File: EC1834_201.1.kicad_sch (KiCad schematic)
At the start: 91 parts, among them X6 RESET_BTN

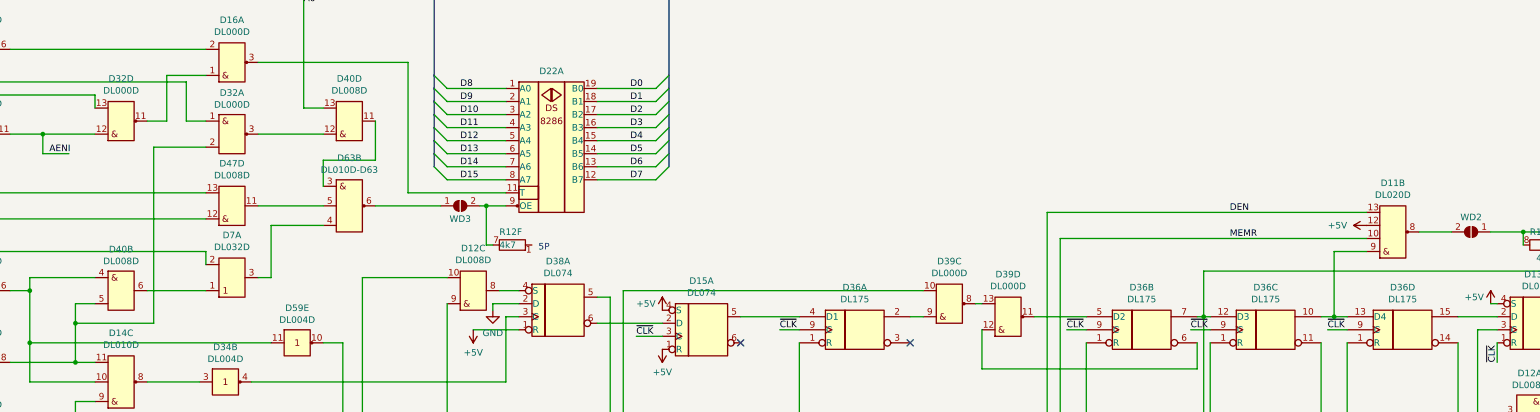
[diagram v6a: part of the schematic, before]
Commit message: Small optical changes
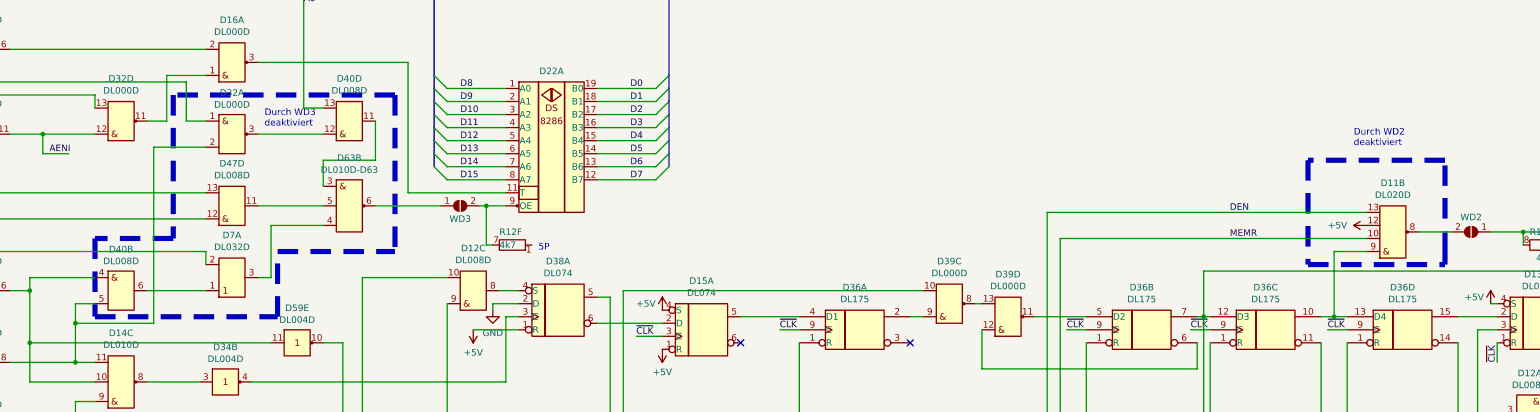
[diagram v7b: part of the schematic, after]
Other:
- note added: "Durch WD2 deaktiviert"
- note added: "Durch WD3 deaktiviert"
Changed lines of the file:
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@@
     (stroke (width 0) (type default) (color 0 0 0 0))
   )
+  (polyline (pts (xy 360.68 62.23) (xy 360.68 82.55))
+    (stroke (width 1) (type dash) (color 132 0 132 1))
+  )
   (wire (pts (xy 162.56 241.3) (xy 222.25 241.3))
     (stroke (width 0) (type default) (color 0 0 0 0))
@@
     (stroke (width 0) (type default) (color 0 0 0 0))
   )
+  (polyline (pts (xy 139.7 49.53) (xy 139.7 77.47))
+    (stroke (width 1) (type dash) (color 168 86 255 1))
+  )
   (wire (pts (xy 81.28 313.69) (xy 123.19 313.69))
     (stroke (width 0) (type default) (color 0 0 0 0))
@@
     (stroke (width 2) (type default) (color 0 0 0 0))
   )
+  (polyline (pts (xy 182.88 49.53) (xy 139.7 49.53))
+    (stroke (width 1) (type dash) (color 168 86 255 1))
+  )
   (wire (pts (xy 217.17 313.69) (xy 217.17 300.99))
     (stroke (width 0) (type default) (color 0 0 0 0))
@@
     (stroke (width 2) (type default) (color 0 0 0 0))
   )
+  (polyline (pts (xy 387.35 80.01) (xy 387.35 62.23))
+    (stroke (width 1) (type dash) (color 132 0 132 1))
+  )
   (bus (pts (xy 219.71 403.86) (xy 264.16 403.86))
     (stroke (width 2) (type default) (color 0 0 0 0))
@@
     (stroke (width 0) (type default) (color 0 0 0 0))
   )
+  (polyline (pts (xy 160.02 80.01) (xy 182.88 80.01))
+    (stroke (width 1) (type dash) (color 168 86 255 1))
+  )
   (bus (pts (xy 518.16 234.95) (xy 518.16 232.41))
     (stroke (width 0.5) (type default) (color 0 0 0 0))
@@
   )
   (wire (pts (xy 185.42 68.58) (xy 185.42 43.18))
-    (stroke (width 0) (type default) (color 0 0 0 0))
+    (stroke (width 0.3) (type default) (color 0 0 0 0))
   )
   (bus (pts (xy 511.81 140.97) (xy 511.81 143.51))
@@
   )
   (wire (pts (xy 185.42 43.18) (xy 156.21 43.18))
-    (stroke (width 0) (type default) (color 0 0 0 0))
+    (stroke (width 0.3) (type default) (color 0 0 0 0))
   )
   (bus (pts (xy 458.47 209.55) (xy 458.47 210.82))
@@
     (stroke (width 2) (type default) (color 0 0 0 0))
   )
+  (polyline (pts (xy 139.7 77.47) (xy 124.46 77.47))
+    (stroke (width 1) (type dash) (color 168 86 255 1))
+  )
   (wire (pts (xy 356.87 248.92) (xy 365.76 248.92))
     (stroke (width 0) (type default) (color 0 0 0 0))
@@
     (stroke (width 0) (type default) (color 0 0 0 0))
   )
+  (polyline (pts (xy 387.35 62.23) (xy 360.68 62.23))
+    (stroke (width 1) (type dash) (color 132 0 132 1))
+  )
   (bus (pts (xy 350.52 241.3) (xy 350.52 243.84))
     (stroke (width 0.5) (type default) (color 0 0 0 0))
@@
     (stroke (width 0.5) (type default) (color 0 0 0 0))
   )
+  (polyline (pts (xy 124.46 92.71) (xy 160.02 92.71))
+    (stroke (width 1) (type dash) (color 168 86 255 1))
+  )
   (wire (pts (xy 242.57 283.21) (xy 255.27 283.21))
     (stroke (width 0) (type default) (color 0 0 0 0))
@@
     (stroke (width 0) (type default) (color 0 0 0 0))
   )
+  (polyline (pts (xy 182.88 49.53) (xy 182.88 80.01))
+    (stroke (width 1) (type dash) (color 168 86 255 1))
+  )
   (wire (pts (xy 142.24 46.99) (xy 95.25 46.99))
     (stroke (width 0) (type default) (color 0 0 0 0))
@@
     (stroke (width 0) (type default) (color 0 0 0 0))
   )
+  (polyline (pts (xy 360.68 82.55) (xy 387.35 82.55))
+    (stroke (width 1) (type dash) (color 132 0 132 1))
+  )
   (bus (pts (xy 346.71 326.39) (xy 346.71 328.93))
     (stroke (width 0.5) (type default) (color 0 0 0 0))
@@
     (stroke (width 0) (type default) (color 0 0 0 0))
   )
+  (polyline (pts (xy 387.35 80.01) (xy 387.35 82.55))
+    (stroke (width 1) (type dash) (color 132 0 132 1))
+  )
   (bus (pts (xy 458.47 207.01) (xy 458.47 208.28))
     (stroke (width 2) (type default) (color 0 0 0 0))
@@
   )
   (wire (pts (xy 204.47 68.58) (xy 185.42 68.58))
-    (stroke (width 0) (type default) (color 0 0 0 0))
+    (stroke (width 0.3) (type default) (color 0 0 0 0))
   )
   (bus (pts (xy 467.36 93.98) (xy 467.36 96.52))
@@
     (stroke (width 0) (type default) (color 0 0 0 0))
   )
+  (polyline (pts (xy 160.02 92.71) (xy 160.02 80.01))
+    (stroke (width 1) (type dash) (color 168 86 255 1))
+  )
   (wire (pts (xy 424.18 160.02) (xy 424.18 129.54))
     (stroke (width 0) (type default) (color 0 0 0 0))
@@
     (stroke (width 0) (type default) (color 0 0 0 0))
   )
+  (polyline (pts (xy 124.46 77.47) (xy 124.46 92.71))
+    (stroke (width 1) (type dash) (color 168 86 255 1))
+  )
   (bus (pts (xy 78.74 93.98) (xy 78.74 101.6))
     (stroke (width 2) (type default) (color 0 0 0 0))
@@
     (effects (font (size 1.27 1.27)) (justify left bottom))
   )
+  (text "Durch WD3\ndeaktiviert" (at 157.48 55.88 0)
+    (effects (font (size 1.27 1.27)) (justify left bottom))
+  )
   (text "X1 Bus Connector auf Seite \"BUS\"" (at 45.72 311.15 90)
     (effects (font (size 8 8)) (justify left bottom))
@@
     (effects (font (size 1.27 1.27)) (justify left bottom))
   )
+  (text "Durch WD2\ndeaktiviert" (at 369.57 59.69 0)
+    (effects (font (size 1.27 1.27)) (justify left bottom))
+  )

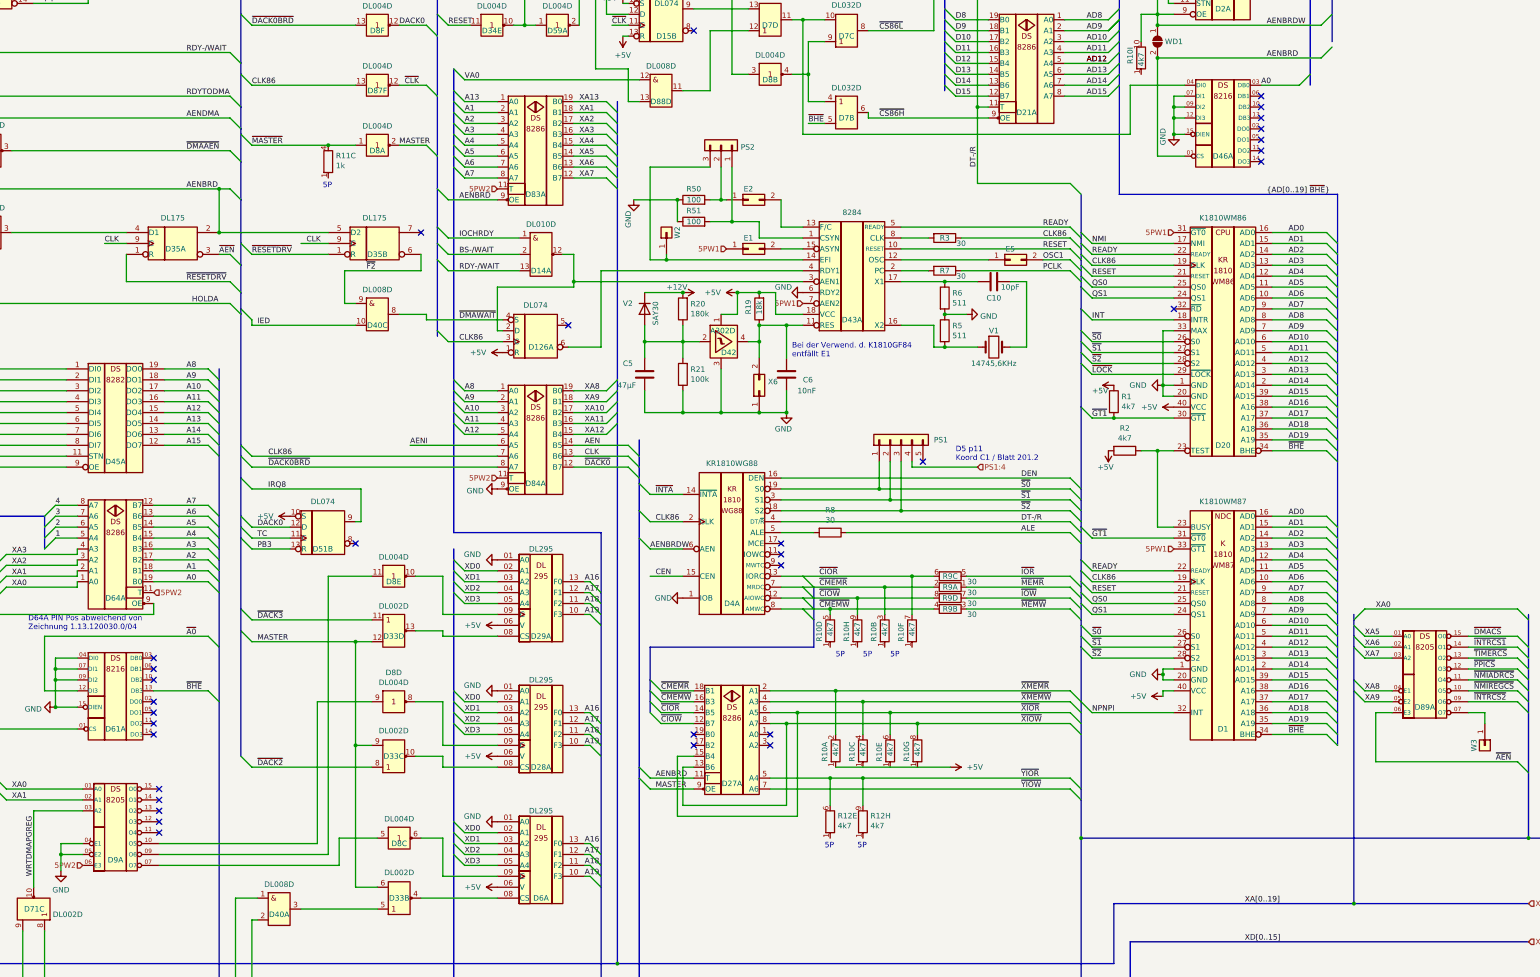
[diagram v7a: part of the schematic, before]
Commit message: Updated some symbol pins no more error on PCB import due to leading zero on pin number also fixed missing network connections added unused pin connections on bus connectors
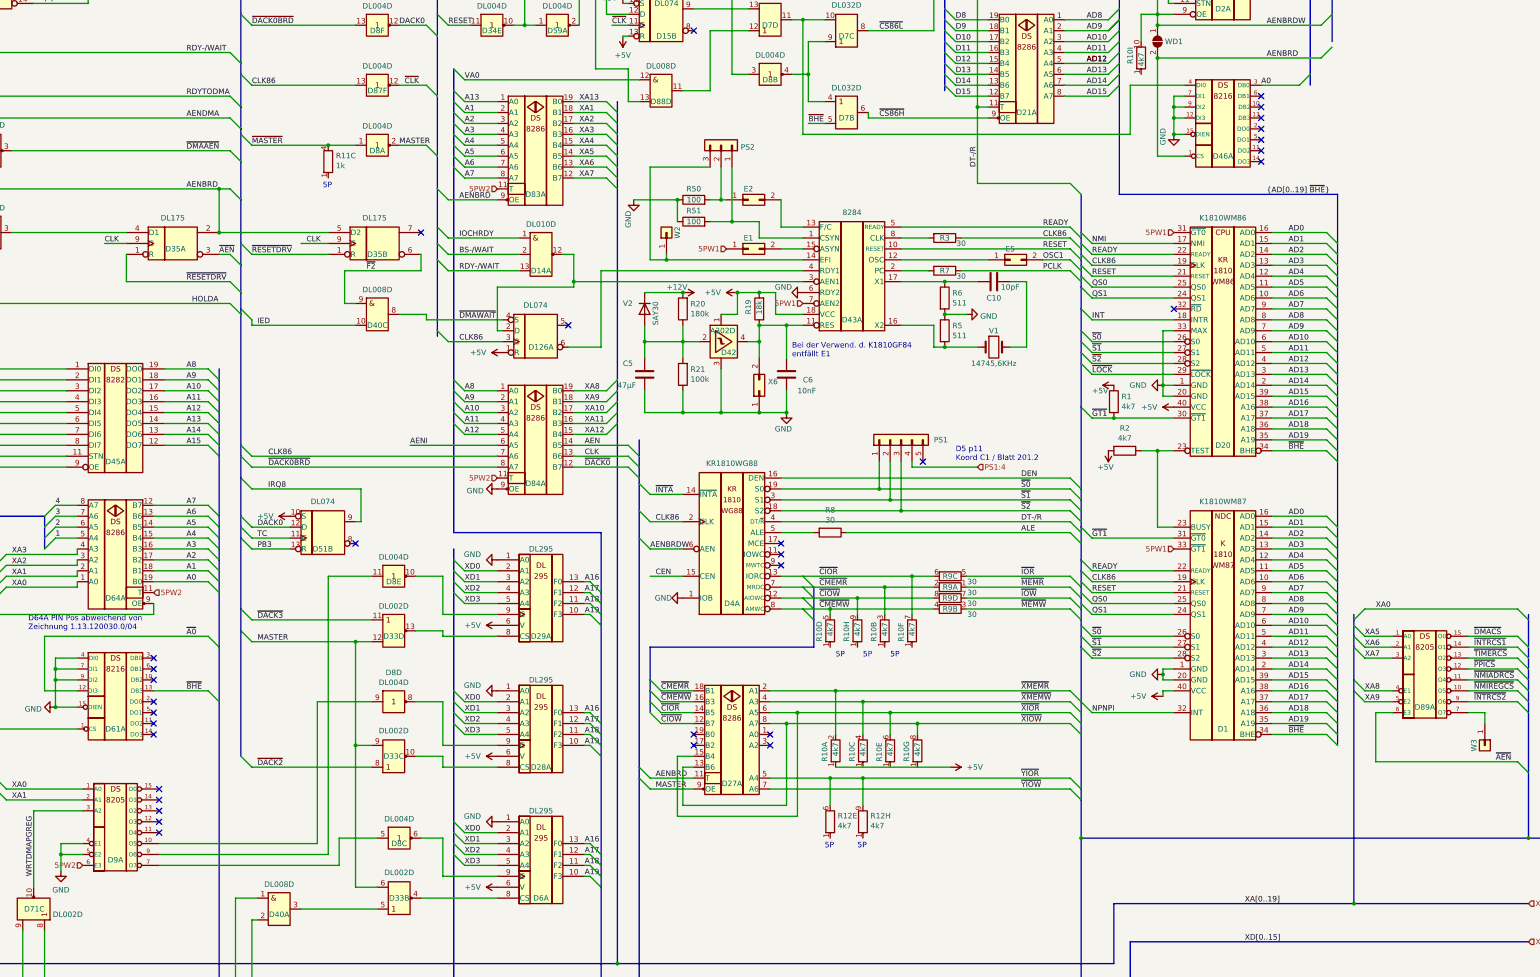
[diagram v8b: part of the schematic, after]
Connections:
- net +5V: now also D28.6 (V), D29.6 (V), D6.6 (V); no longer D28.06 (V), D29.06 (V), D6.06 (V)
- net 5PW2: now also D9.6 (E3); no longer D9.06 (E3)
- net A0: now also D46.3 (DB0); no longer D46.03 (DB0)
- net AENBRD: now also D46.1 (CS); no longer D46.01 (CS)
- net GND: now also D28.1 (A0), D29.1 (A0), D46.7 (DI1), D46.9 (DI2), D6.1 (A0), D61.4 (DI0), D61.7 (DI1), D61.9 (DI2), D9.4 (E1), D9.5 (E2); no longer D28.01 (A0), D29.01 (A0), D46.07 (DI1), D46.09 (DI2), D6.01 (A0), D61.04 (DI0), D61.07 (DI1), D61.09 (DI2), D9.04 (E1), D9.05 (E2)
- net WRTDMAPGREG: now also D9.3 (A2); no longer D9.03 (A2)
- net XA0: now also D9.1 (A0); no longer D9.01 (A0)
- net XA1: now also D9.2 (A1); no longer D9.02 (A1)
- net XA5: now also D89.1 (A0); no longer D89.01 (A0)
- net XA6: now also D89.2 (A1); no longer D89.02 (A1)
- net XA7: now also D89.3 (A2); no longer D89.03 (A2)
- net XA8: now also D89.4 (E1); no longer D89.04 (E1)
- net XA9: now also D89.5 (E2); no longer D89.05 (E2)
- net XD0: now also D28.2 (A1), D29.2 (A1), D6.2 (A1); no longer D28.02 (A1), D29.02 (A1), D6.02 (A1)
- net XD1: now also D28.3 (A2), D29.3 (A2), D6.3 (A2); no longer D28.03 (A2), D29.03 (A2), D6.03 (A2)
- net XD2: now also D28.4 (A3), D29.4 (A3), D6.4 (A3); no longer D28.04 (A3), D29.04 (A3), D6.04 (A3)
- net XD3: now also D28.5 (A4), D29.5 (A4), D6.5 (A4); no longer D28.05 (A4), D29.05 (A4), D6.05 (A4)
- net ~{AEN}: now also D89.6 (E3); no longer D89.06 (E3)
- net ~{INTRCS2}: now also D89.9 (O6); no longer D89.09 (O6)
- net at W3.1 (Pin_1): now also D89.7 (O7); no longer D89.07 (O7)
- net at D7.10 (B3), D7.11 (Y4): now also D46.4 (DI0); no longer D46.04 (DI0)
- net at D33.4 (Y2): now also D6.8 (CS); no longer D6.08 (CS)
- net at D8.6 (Y3): now also D6.9 (C); no longer D6.09 (C)
- net at D33.10 (Y3): now also D28.8 (CS); no longer D28.08 (CS)
- net at D8.8 (Y4): now also D28.9 (C); no longer D28.09 (C)
- net at D33.13 (Y4): now also D29.8 (CS); no longer D29.08 (CS)
- net at D8.10 (Y5): now also D29.9 (C); no longer D29.09 (C)
- net at D8.5 (A3): now also D9.7 (O7); no longer D9.07 (O7)
- net at D8.11 (A5): now also D9.9 (O6); no longer D9.09 (O6)
- net at D45.9 (OE), D62.3 (Y1), D64.9 (OE): now also D61.1 (CS); no longer D61.01 (CS)
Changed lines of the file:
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@@
     (stroke (width 0) (type default) (color 0 0 0 0))
   )
+  (wire (pts (xy 314.96 346.71) (xy 322.58 346.71))
+    (stroke (width 0) (type default) (color 0 0 0 0))
+  )
   (wire (pts (xy 222.25 55.88) (xy 233.68 55.88))
     (stroke (width 0) (type default) (color 0 0 0 0))
@@
     (stroke (width 0) (type default) (color 0 0 0 0))
   )
-  (wire (pts (xy 314.96 346.71) (xy 322.58 346.71))
-    (stroke (width 0) (type default) (color 0 0 0 0))
-  )
   (wire (pts (xy 162.56 151.13) (xy 157.48 151.13))
     (stroke (width 0) (type default) (color 0 0 0 0))
@@
       (effects (font (size 1.27 1.27)) hide)
     )
-    (pin "01")
-    (pin "02")
-    (pin "03")
-    (pin "04")
-    (pin "05")
-    (pin "06")
-    (pin "07")
-    (pin "09")
+    (pin "1")
     (pin "10")
     (pin "11")
@@
     (pin "14")
     (pin "15")
+    (pin "2")
+    (pin "3")
+    (pin "4")
+    (pin "5")
+    (pin "6")
+    (pin "7")
+    (pin "9")
     (pin "16")
     (pin "8")
@@
       (effects (font (size 1.27 1.27)) hide)
     )
-    (pin "01")
-    (pin "02")
-    (pin "03")
-    (pin "04")
-    (pin "05")
-    (pin "06")
-    (pin "07")
-    (pin "09")
+    (pin "1")
     (pin "10")
     (pin "11")
@@
     (pin "14")
     (pin "15")
+    (pin "2")
+    (pin "3")
+    (pin "4")
+    (pin "5")
+    (pin "6")
+    (pin "7")
+    (pin "9")
     (pin "16")
     (pin "8")
@@
       (effects (font (size 1.27 1.27)) hide)
     )
-    (pin "01")
-    (pin "02")
-    (pin "03")
-    (pin "04")
-    (pin "05")
-    (pin "06")
-    (pin "08")
-    (pin "09")
+    (pin "1")
     (pin "10")
     (pin "11")
     (pin "12")
     (pin "13")
+    (pin "2")
+    (pin "3")
+    (pin "4")
+    (pin "5")
+    (pin "6")
+    (pin "8")
+    (pin "9")
     (pin "14")
     (pin "7")
@@
       (effects (font (size 1.27 1.27)) hide)
     )
-    (pin "01")
-    (pin "02")
-    (pin "03")
-    (pin "04")
-    (pin "05")
-    (pin "06")
-    (pin "08")
-    (pin "09")
+    (pin "1")
     (pin "10")
     (pin "11")
     (pin "12")
     (pin "13")
+    (pin "2")
+    (pin "3")
+    (pin "4")
+    (pin "5")
+    (pin "6")
+    (pin "8")
+    (pin "9")
     (pin "14")
     (pin "7")
   )
-  (symbol (lib_name "DL295_2") (lib_id "robotron_ec1834:DL295") (at 332.74 292.1 0) (unit 1)
+  (symbol (lib_id "robotron_ec1834:DL295") (at 332.74 292.1 0) (unit 1)
     (in_bom yes) (on_board yes)
     (property "Reference" "D29" (id 0) (at 332.74 300.99 0))
@@
       (effects (font (size 1.27 1.27)) hide)
     )
-    (pin "01")
-    (pin "02")
-    (pin "03")
-    (pin "04")
-    (pin "05")
-    (pin "06")
-    (pin "08")
-    (pin "09")
+    (pin "1")
     (pin "10")
     (pin "11")
     (pin "12")
     (pin "13")
+    (pin "2")
+    (pin "3")
+    (pin "4")
+    (pin "5")
+    (pin "6")
+    (pin "8")
+    (pin "9")
     (pin "14")
     (pin "7")
@@
     (pin "7")
   )
-  (symbol (lib_id "robotron_ec1834:DS8205") (at 233.68 345.44 0) (unit 1)
+  (symbol (lib_name "DS8205_1") (lib_id "robotron_ec1834:DS8205") (at 233.68 345.44 0) (unit 1)
     (in_bom yes) (on_board yes)
     (property "Reference" "D9" (id 0) (at 233.68 353.06 0))
@@
       (effects (font (size 1.27 1.27)) hide)
     )
-    (pin "01")
-    (pin "02")
-    (pin "03")
-    (pin "04")
-    (pin "05")
-    (pin "06")
-    (pin "07")
-    (pin "09")
+    (pin "1")
     (pin "10")
     (pin "11")
@@
     (pin "14")
     (pin "15")
+    (pin "2")
+    (pin "3")
+    (pin "4")
+    (pin "5")
+    (pin "6")
+    (pin "7")
+    (pin "9")
     (pin "16")
     (pin "8")
   )
-  (symbol (lib_id "robotron_ec1834:DS8216") (at 233.68 314.96 0) (unit 1)
+  (symbol (lib_name "DS8216_1") (lib_id "robotron_ec1834:DS8216") (at 233.68 314.96 0) (unit 1)
     (in_bom yes) (on_board yes)
     (property "Reference" "D61" (id 0) (at 233.68 322.58 0))
@@
       (effects (font (size 1.27 1.27)) hide)
     )
-    (pin "01")
-    (pin "02")
-    (pin "03")
-    (pin "04")
-    (pin "05")
-    (pin "06")
-    (pin "07")
-    (pin "09")
+    (pin "1")
     (pin "10")
     (pin "11")
@@
     (pin "14")
     (pin "15")
+    (pin "2")
+    (pin "3")
+    (pin "4")
+    (pin "5")
+    (pin "6")
+    (pin "7")
+    (pin "9")
     (pin "16")
     (pin "8")
